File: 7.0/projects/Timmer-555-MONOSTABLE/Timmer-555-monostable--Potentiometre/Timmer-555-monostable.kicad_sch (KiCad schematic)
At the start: 10 parts, among them SW0 SW_SWITCH, U1 LM555xM

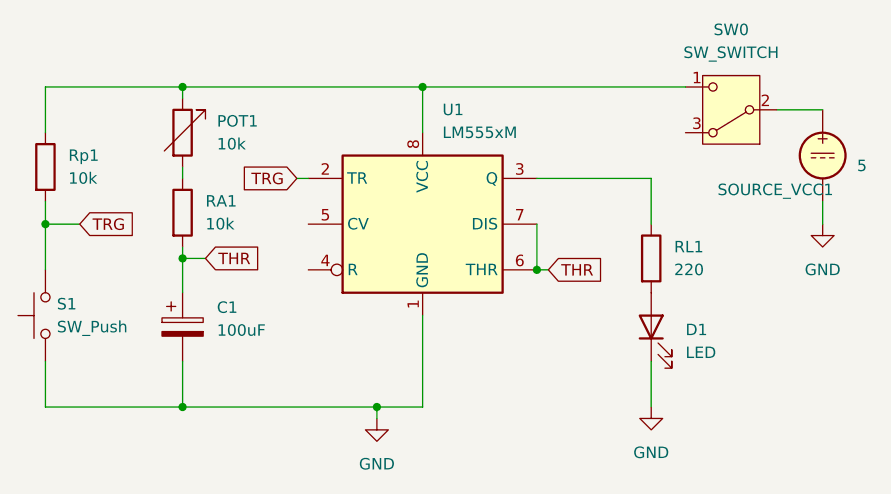
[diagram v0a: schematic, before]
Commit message: adding timmer 555
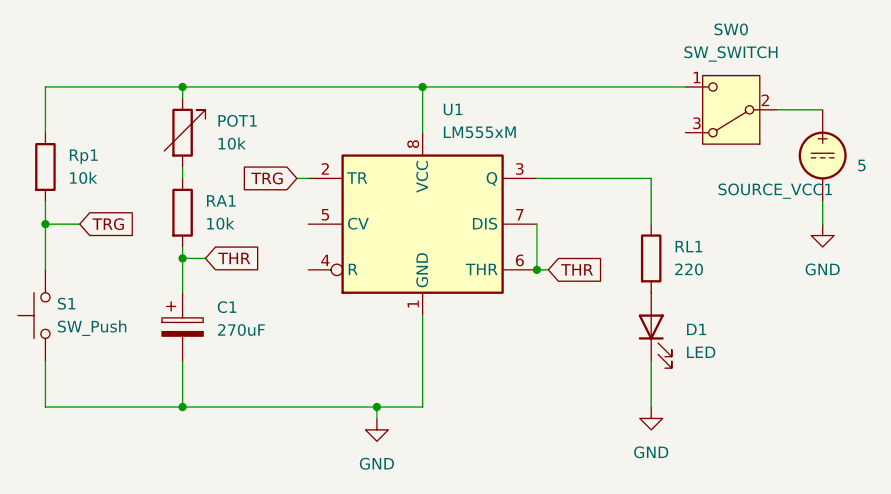
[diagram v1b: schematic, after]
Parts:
- C1: value 100uF -> 270uF
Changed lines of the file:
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@@
 			)
 		)
-		(property "Value" "100uF"
+		(property "Value" "270uF"
 			(at 87.63 94.3609 0)
 			(effects
